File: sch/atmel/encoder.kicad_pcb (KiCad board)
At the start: 2 copper layers, 100 x 100 mm, 71 parts, among them J1 GND-24V, J2 ENCODER, J3 ICSP, J4 CAN, Q1 BC817, Q2 MMBT2222A, U1 ATMEGA328P-PU, U2 DS1307, U3 LM7805CV, U4 PSW-8,5R, U5 PESD1CAN, U6 MPC2551, U7 MCP2515-E/SO, U8 MAX485CSA, Y1 16MHz, Y2 32.768KHz, Y3 16MHz

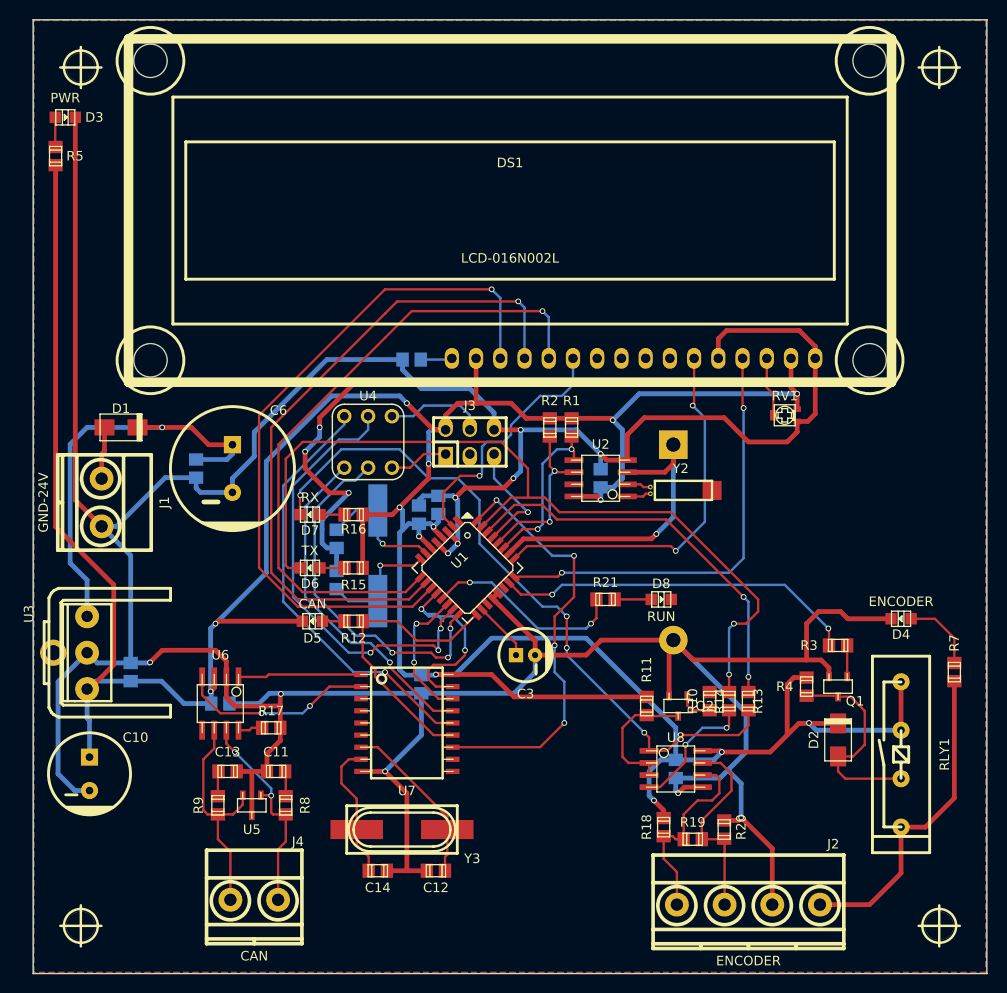
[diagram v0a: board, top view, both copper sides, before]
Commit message: regulador tensao d2pak
Signed-off-by: cuki2 <mauricio@krebs.com.br>
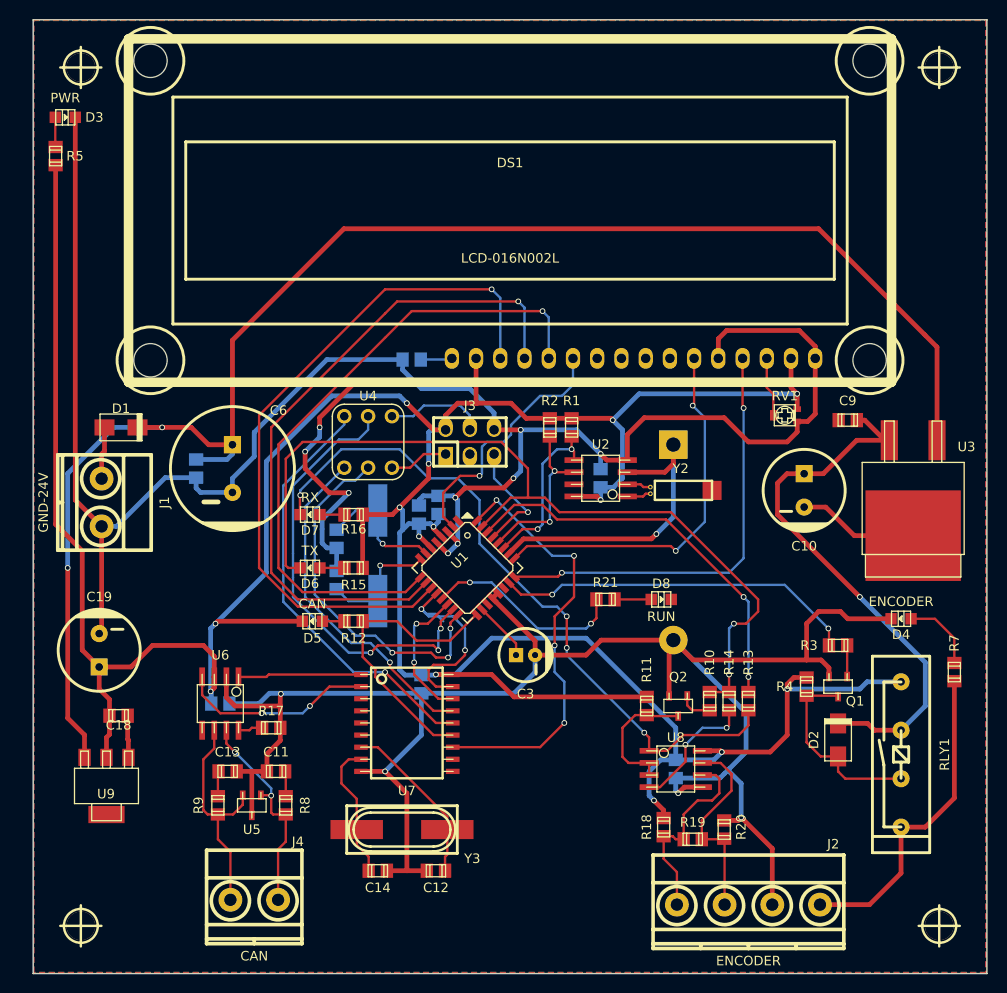
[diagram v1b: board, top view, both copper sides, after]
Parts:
- added C18: 100nF 50V, w_smd_cap:c_0805, F.Cu at (29.0, 93.0)
- added C19: 470uF 10V, w_capacitors:CP_8x11.5mm, F.Cu at (26.9, 86.1)
- added U9: LD1117S50TR, w_smd_trans:sot223, F.Cu at (27.7, 100.3)
- C9: moved to F.Cu
- U3: value LM7805CV -> L7805CD2T; footprint w_to:to220_5772 -> w_smd_trans:d2-pak
- moved U3 88.3 mm to (112.3, 69.1), turned to 180 degrees
- moved C10 80.6 mm to (100.8, 69.3)
- moved C9 79.7 mm to (105.4, 62.0), turned to 0 degrees
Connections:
- C1 pad 1: +5V -> Net-(C1-Pad1)
- C1 pad 2: GND -> Net-(C1-Pad2)
- C10 pad 1: +5V -> +5C
- C9 pad 1: +5V -> +5C
- D2 pad 2: +5V -> +5C
- RLY1 pad 5: +5V -> +5C
- U1 pad 26: +BATT -> Net-(U1-Pad26)
- U3 pad 3: +5V -> +5C
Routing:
- net Net-(C6-Pad1): track 44.9 -> 162.7 mm, vias 1 -> 2
- net +5C: track 0.00 -> 58.4 mm, vias 0 -> 1
- net GND: track 471.7 -> 447.6 mm, vias 15 -> 14
- net +5V: track 368.4 -> 355.8 mm
- net Net-(C1-Pad1): track 0.00 -> 3.62 mm
- net Net-(U1-Pad26): track 0.00 -> 2.21 mm
- net +BATT: track 33.7 -> 31.5 mm
- net Net-(D2-Pad1): track 22.1 -> 20.6 mm
- net Net-(C1-Pad2): track 0.00 -> 1.20 mm

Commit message: Signed-off-by: cuki2 <mauricio@krebs.com.br>
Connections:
- C1 pad 1: Net-(C1-Pad1) -> +5V
- C1 pad 2: Net-(C1-Pad2) -> GND
- U1 pad 26: Net-(U1-Pad26) -> +BATT
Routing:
- net +5V: track 355.8 -> 359.4 mm
- net Net-(C1-Pad1): track 3.62 -> 0.00 mm
- net Net-(U1-Pad26): track 2.21 -> 0.00 mm
- net +BATT: track 31.5 -> 33.7 mm
- net Net-(C1-Pad2): track 1.20 -> 0.00 mm
- net GND: track 447.6 -> 448.8 mm

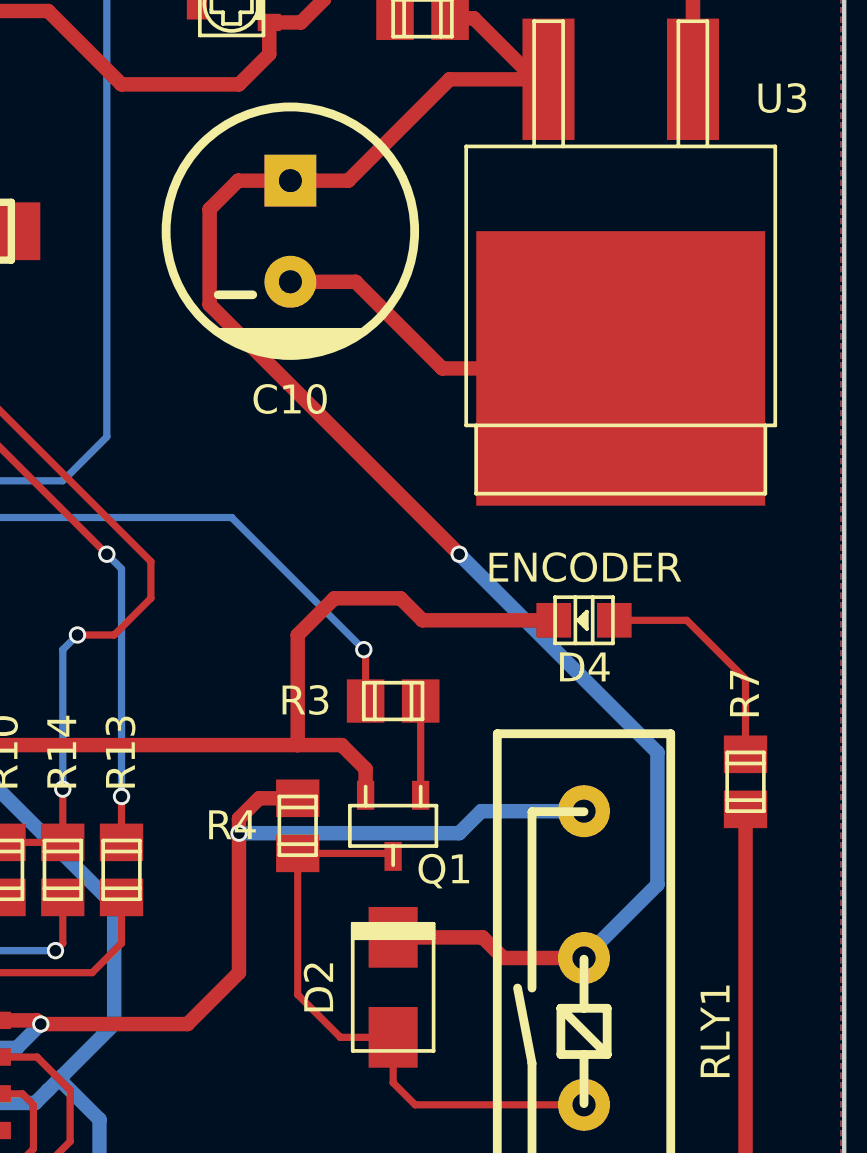
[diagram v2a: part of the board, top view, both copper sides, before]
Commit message: correcao rele alimentacao encoder
Signed-off-by: cuki2 <mauricio@krebs.com.br>
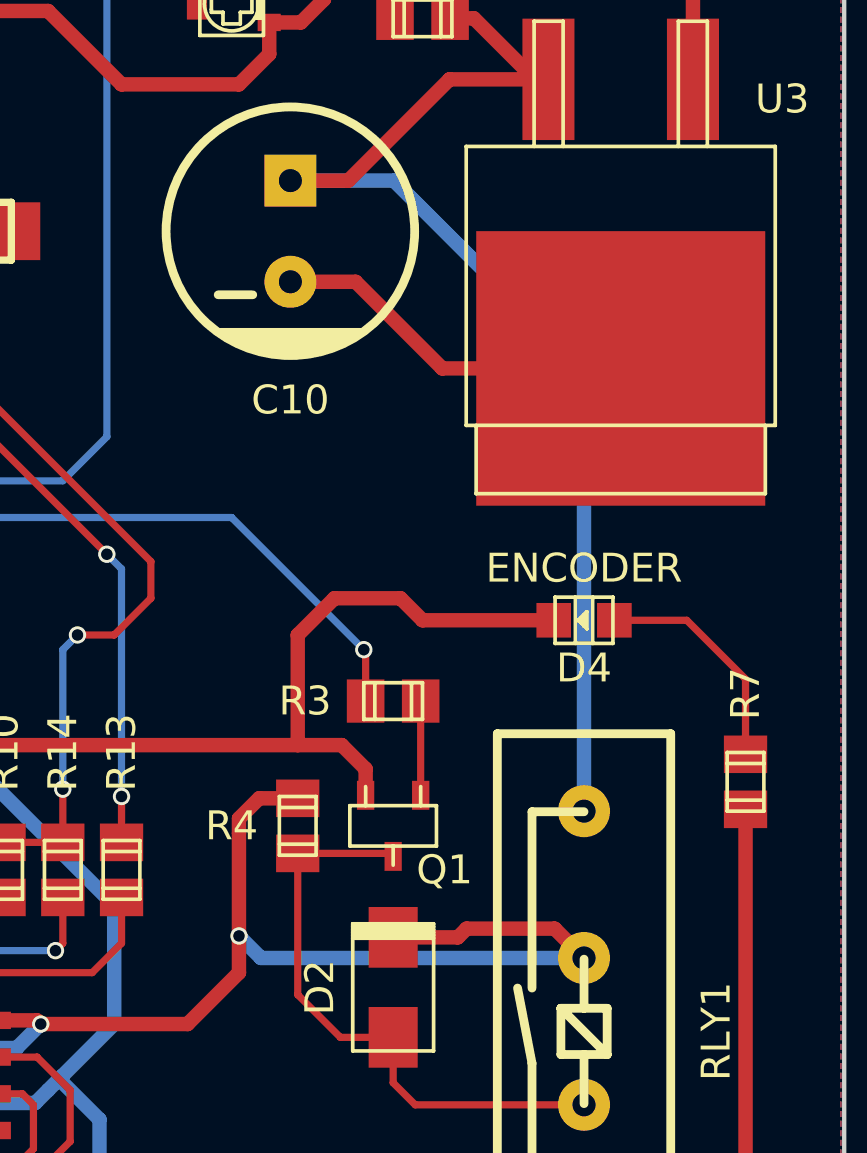
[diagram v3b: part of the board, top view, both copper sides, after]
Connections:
- D2 pad 2: +5C -> +5V
- RLY1 pad 5: +5C -> +5V
- RLY1 pad 7: +5V -> +5C
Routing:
- net +5C: track 58.4 -> 42.8 mm, vias 1 -> 0
- net +5V: track 359.4 -> 366.6 mm
